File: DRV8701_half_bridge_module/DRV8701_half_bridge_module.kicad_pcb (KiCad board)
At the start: 2 copper layers, 45 x 23.5 mm, 22 parts, among them J1 1x8 2.54, J2 1x8 2.54, J3 1x2 5.08, Q1 NMOS, Q2 NMOS, U1 DRV8701E

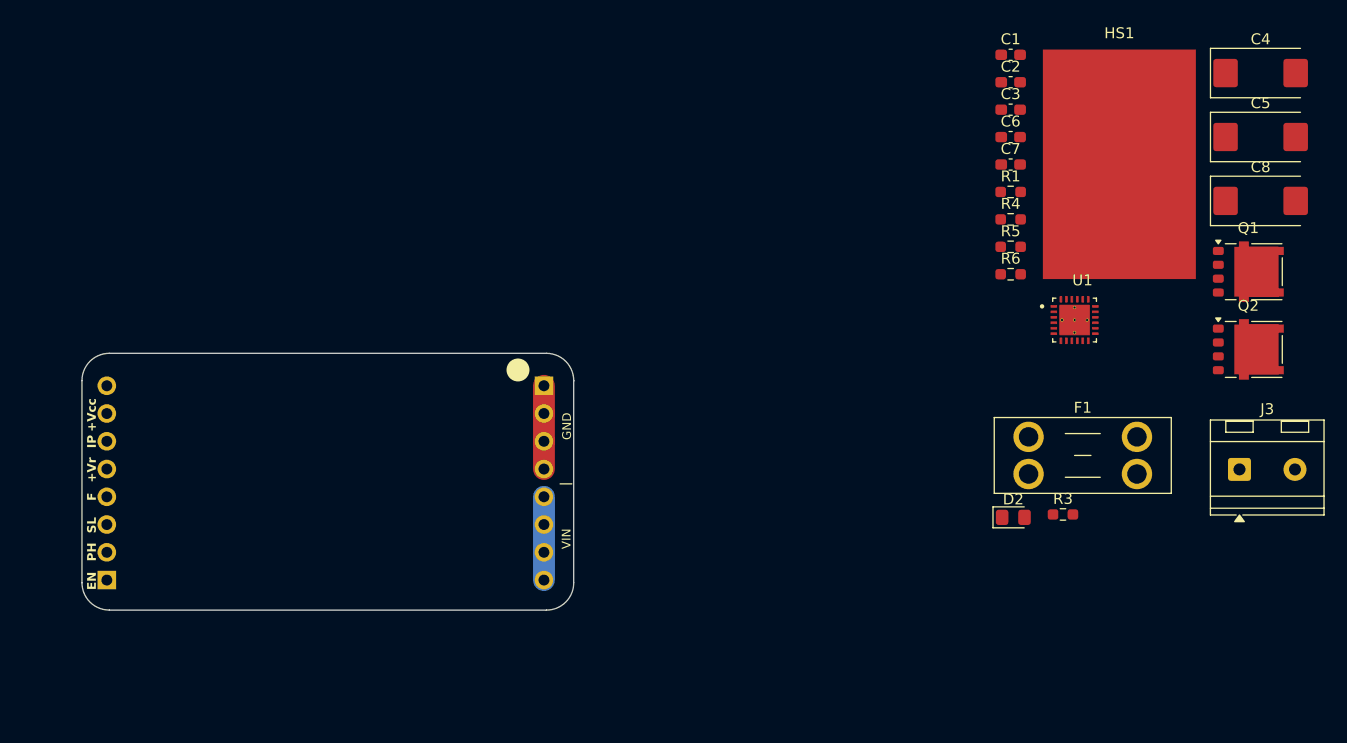
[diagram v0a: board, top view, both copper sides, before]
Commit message: Half bridge layout with errors
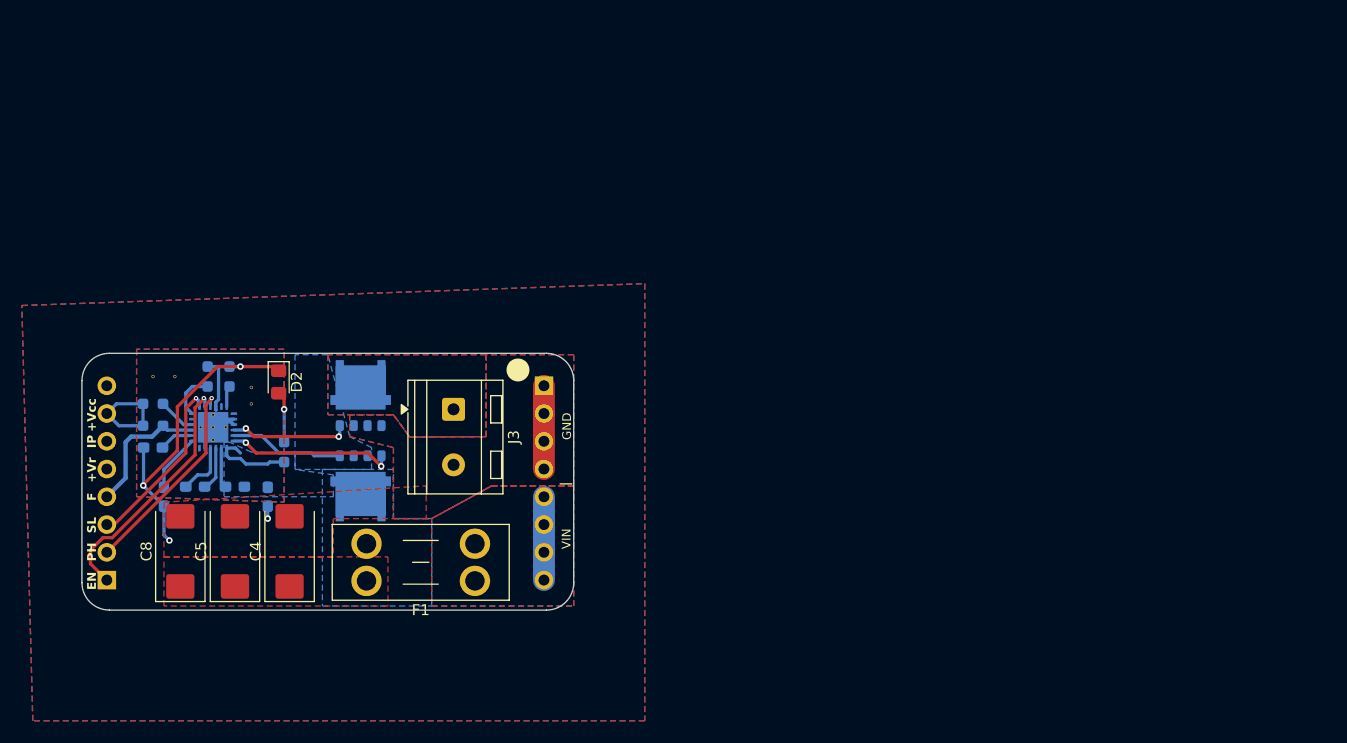
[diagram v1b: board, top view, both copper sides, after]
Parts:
- removed HS1: Heatsink, heatsinks:DRV8874_TO220_Heatsink
- added ?: , , F.Cu at (63.5, 63.0)
- added ?: , , F.Cu at (56.5, 60.5)
- added ?: , , F.Cu at (63.5, 61.5)
- added ?: , , F.Cu at (54.5, 60.5)
- C1, C2, C3, C6, C7, Q1, Q2, R1, R3, R4, R5, R6, U1: moved to B.Cu
- moved C8 103.9 mm to (57.0, 76.5), turned to 90 degrees
- moved C5 101.2 mm to (62.0, 76.5), turned to 90 degrees
- moved C4 99.1 mm to (67.0, 76.5), turned to 90 degrees
- moved C1 87.4 mm to (55.5, 71.5), turned to 90 degrees
- moved Q1 83.6 mm to (73.5, 70.5), turned to -90 degrees
- moved C2 83.3 mm to (58.4, 70.6), turned to 180 degrees
- moved C7 82.6 mm to (54.5, 67.0)
- moved R1 81.3 mm to (54.5, 65.0)
- moved Q2 81.3 mm to (73.5, 62.2), turned to 90 degrees
- moved U1 79.4 mm to (60.0, 65.2), turned to 90 degrees
- moved R6 79.4 mm to (54.5, 63.0)
- moved C6 77.9 mm to (62.0, 70.6), turned to 180 degrees
- moved C3 76.7 mm to (65.0, 71.5), turned to -90 degrees
- moved R5 74.4 mm to (59.5, 60.5), turned to 90 degrees
- moved R4 72.9 mm to (61.5, 60.5), turned to -90 degrees
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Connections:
- U1 pad 26: (no net) -> GND
- U1 pad 27: (no net) -> GND
- U1 pad 28: (no net) -> GND
- U1 pad 29: (no net) -> GND
- U1 pad 30: (no net) -> GND
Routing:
- net GND: track 7.62 -> 49.9 mm, vias 0 -> 4
- net /Motor driver/EN: track 0.00 -> 22.9 mm, vias 0 -> 1
- net /Motor driver/PH: track 0.00 -> 18.7 mm, vias 0 -> 1
- net /Motor driver/SLEEP: track 0.06 -> 16.3 mm, vias 0 -> 1
- net Net-(Q1-G): track 0.00 -> 15.4 mm, vias 0 -> 2
- net /Motor driver/FAULT: track 0.71 -> 13.3 mm
- net Net-(Q2-G): track 0.00 -> 11.0 mm, vias 0 -> 2
- net /Motor driver/OUT1: track 0.00 -> 10.5 mm
- net +Vcc: track 0.00 -> 9.45 mm
- net +VM: track 0.00 -> 7.77 mm
- net Net-(U1-AVDD): track 0.00 -> 5.31 mm
- net Net-(U1-CPL): track 0.00 -> 5.00 mm
- net Net-(D2-A): track 0.00 -> 4.68 mm, vias 0 -> 1
- net Net-(U1-IDRIVE): track 0.00 -> 4.39 mm
- net Net-(U1-CPH): track 0.00 -> 4.07 mm
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- added copper zone on B.Cu, net (none)
- added copper zone on F.Cu, net (none)
- added copper zone on B.Cu, net +VM
- added copper zone on F.Cu, net +VM
- added copper zone on B.Cu, net /Motor driver/OUT1
- added copper zone on F.Cu, net /Motor driver/OUT1
- added copper zone on B.Cu, net /Power supply/Vin
- added copper zone on F.Cu, net /Power supply/Vin
- added copper zone on B.Cu, net GND
- added copper zone on F.Cu, net GND

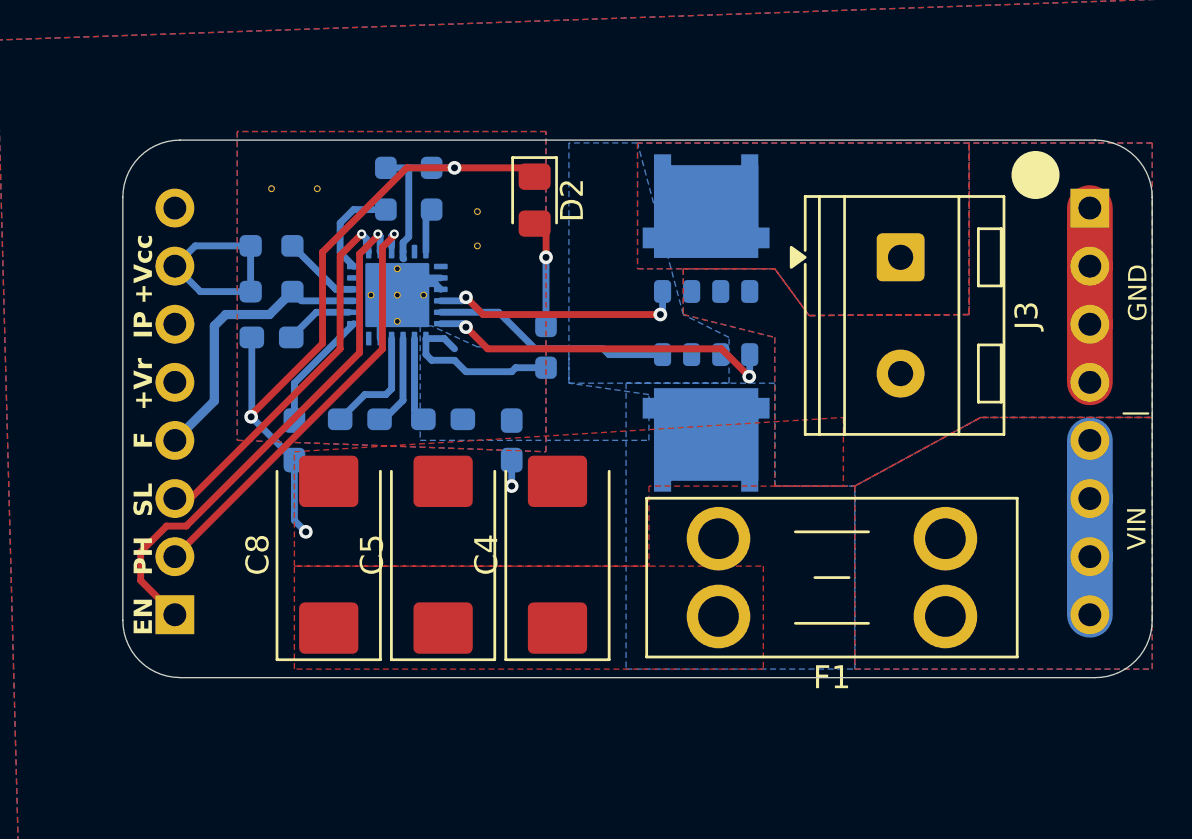
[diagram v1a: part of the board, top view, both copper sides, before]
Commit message: Half bridge error fixed
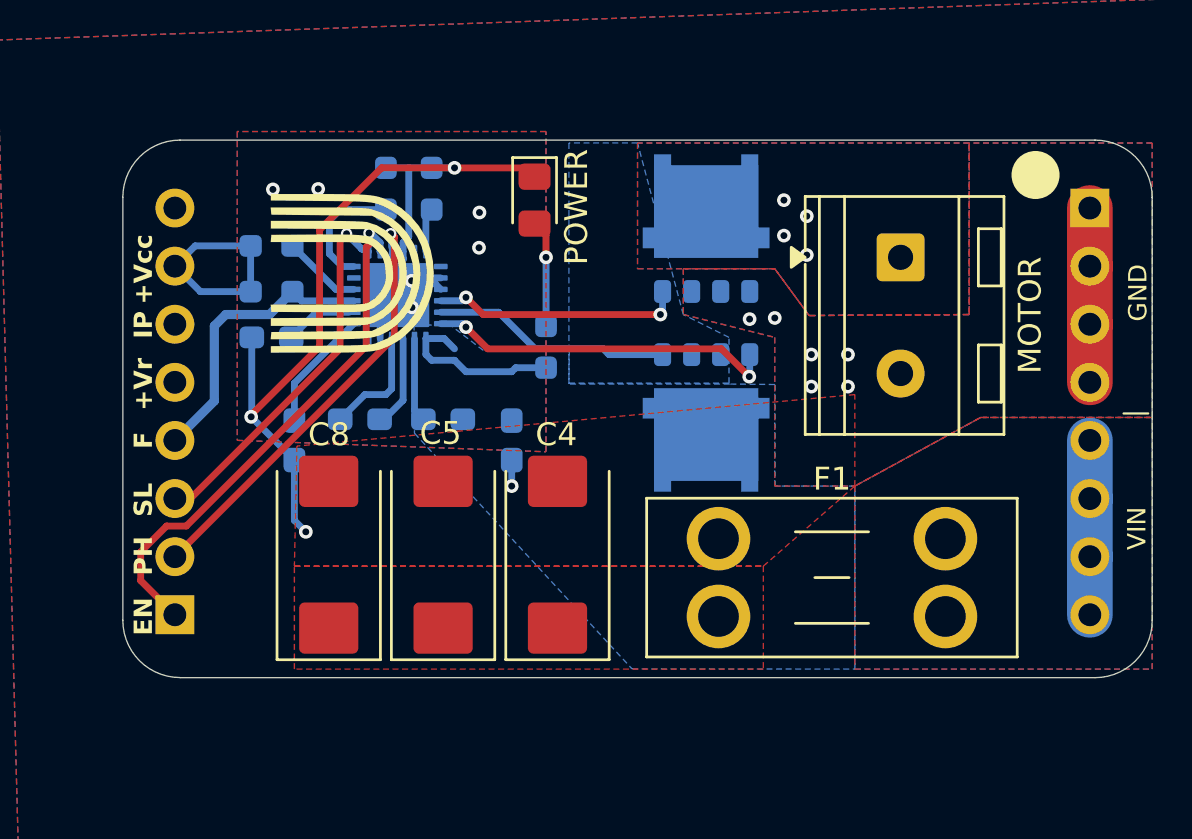
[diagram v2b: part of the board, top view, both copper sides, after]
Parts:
- removed ? (x4): , 
- added G***: LOGO, LOGO, F.Cu at (62.0, 64.2)
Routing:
- net Net-(U1-IDRIVE): track 4.39 -> 5.42 mm
- net GND: track 49.9 -> 49.6 mm, vias 4 -> 16
- net /Motor driver/OUT1: vias 0 -> 4
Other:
- board text added: "DRV8701 half bridge module v1.0.0"
- board text added: "MOTOR"
- board text added: "POWER"
